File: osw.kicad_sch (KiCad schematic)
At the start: 59 parts, among them J1 Conn_01x02, J2 microSD_MEM2067-02-180-00-A_R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, J3 2169890001, Q1 Q_NMOS_ToshibaSMD, SW1 SPST_EVQ-P7J01P, SW2 SPST_EVQ-P7J01P, SW3 SPST_EVQ-P7J01P, SW4 SPST_EVQ-P7J01P, U1 L96-M33, U10 BMA400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

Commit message: working on the layout.
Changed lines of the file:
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@@
-    (stroke (width 0) (type default))
-  )
-  (wire (pts (xy 88 105) (xy 88 107))
-    (stroke (width 0) (type default))
-  )
-  (wire (pts (xy 88 119) (xy 88 121))
     (stroke (width 0) (type default))
   )

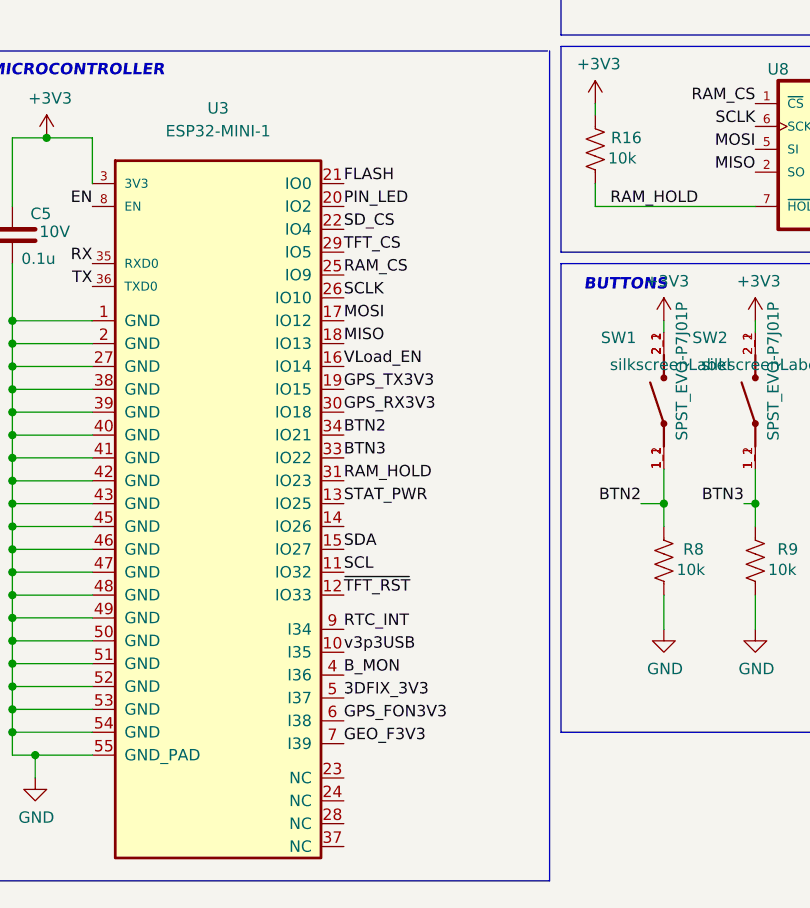
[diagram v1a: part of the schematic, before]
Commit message: Repinned out the ESP32 to get a bit better layout.
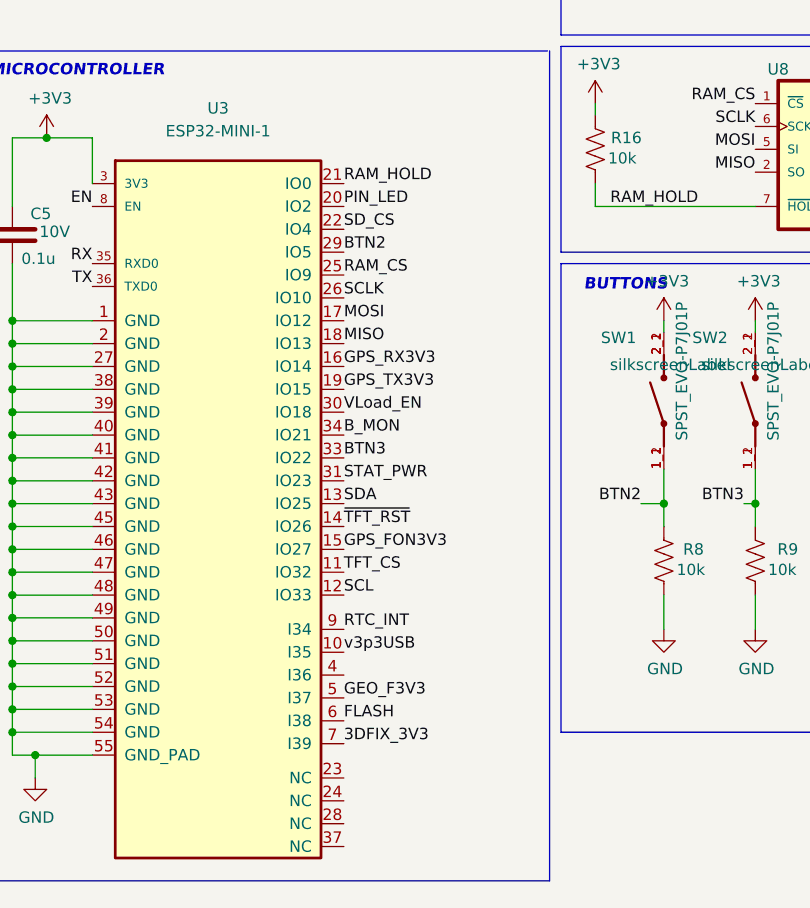
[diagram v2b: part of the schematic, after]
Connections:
- net 3DFIX_3V3: now also U3.7 (I39); no longer U3.5 (I37)
- net BTN2: now also U3.29 (IO5); no longer U3.34 (IO21)
- net B_MON: now also U3.34 (IO21); no longer U3.4 (I36)
- net FLASH: now also U3.6 (I38); no longer U3.21 (IO0)
- net GEO_F3V3: now also U3.5 (I37); no longer U3.7 (I39)
- net GPS_FON3V3: now also U3.15 (IO27); no longer U3.6 (I38)
- net GPS_RX3V3: now also U3.16 (IO14); no longer U3.30 (IO18)
- net RAM_HOLD: now also U3.21 (IO0); no longer U3.31 (IO23)
- net SCL: now also U3.12 (IO33); no longer U3.11 (IO32)
- net SDA: now also U3.13 (IO25); no longer U3.15 (IO27)
- net STAT_PWR: now also U3.31 (IO23); no longer U3.13 (IO25)
- net TFT_CS: now also U3.11 (IO32); no longer U3.29 (IO5)
- net VLoad_EN: now also U3.30 (IO18); no longer U3.16 (IO14)
- net ~{TFT_RST}: now also U3.14 (IO26); no longer U3.12 (IO33)
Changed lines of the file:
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@@
     (effects (font (size 1.27 1.27) (thickness 0.254) bold italic) (justify left bottom))
   )
-  (label "~{TFT_RST}" (at 119.38 124.46 0) (fields_autoplaced)
+  (label "~{TFT_RST}" (at 119.38 116.84 0) (fields_autoplaced)
     (effects (font (size 1.27 1.27)) (justify left bottom))
   )
@@
     (effects (font (size 1.27 1.27)) (justify left bottom))
   )
-  (label "SDA" (at 119.38 119.38 0) (fields_autoplaced)
+  (label "SDA" (at 119.38 114.3 0) (fields_autoplaced)
     (effects (font (size 1.27 1.27)) (justify left bottom))
   )
@@
     (effects (font (size 1.27 1.27)) (justify left bottom))
   )
-  (label "3DFIX_3V3" (at 119.38 135.89 0) (fields_autoplaced)
+  (label "3DFIX_3V3" (at 119.38 140.97 0) (fields_autoplaced)
     (effects (font (size 1.27 1.27)) (justify left bottom))
   )
@@
     (effects (font (size 1.27 1.27)) (justify right bottom))
   )
-  (label "B_MON" (at 119.38 133.35 0) (fields_autoplaced)
+  (label "B_MON" (at 119.38 106.68 0) (fields_autoplaced)
     (effects (font (size 1.27 1.27)) (justify left bottom))
   )
@@
     (effects (font (size 1.27 1.27)) (justify right bottom))
   )
-  (label "VLoad_EN" (at 119.38 99.06 0) (fields_autoplaced)
-    (effects (font (size 1.27 1.27)) (justify left bottom))
-  )
-  (label "GPS_FON3V3" (at 119.38 138.43 0) (fields_autoplaced)
+  (label "VLoad_EN" (at 119.38 104.14 0) (fields_autoplaced)
+    (effects (font (size 1.27 1.27)) (justify left bottom))
+  )
+  (label "GPS_FON3V3" (at 119.38 119.38 0) (fields_autoplaced)
     (effects (font (size 1.27 1.27)) (justify left bottom))
   )
@@
     (effects (font (size 1.27 1.27)) (justify right bottom))
   )
-  (label "SCL" (at 119.38 121.92 0) (fields_autoplaced)
-    (effects (font (size 1.27 1.27)) (justify left bottom))
-  )
-  (label "GEO_F3V3" (at 119.38 140.97 0) (fields_autoplaced)
+  (label "SCL" (at 119.38 124.46 0) (fields_autoplaced)
+    (effects (font (size 1.27 1.27)) (justify left bottom))
+  )
+  (label "GEO_F3V3" (at 119.38 135.89 0) (fields_autoplaced)
     (effects (font (size 1.27 1.27)) (justify left bottom))
   )
@@
     (effects (font (size 1.27 1.27)) (justify left bottom))
   )
-  (label "GPS_RX3V3" (at 119.38 104.14 0) (fields_autoplaced)
+  (label "GPS_RX3V3" (at 119.38 99.06 0) (fields_autoplaced)
     (effects (font (size 1.27 1.27)) (justify left bottom))
   )
@@
     (effects (font (size 1.27 1.27)) (justify right bottom))
   )
-  (label "TFT_CS" (at 119.38 86.36 0) (fields_autoplaced)
+  (label "TFT_CS" (at 119.38 121.92 0) (fields_autoplaced)
     (effects (font (size 1.27 1.27)) (justify left bottom))
   )
@@
     (effects (font (size 1.27 1.27)) (justify right bottom))
   )
-  (label "RAM_HOLD" (at 119.38 111.76 0) (fields_autoplaced)
+  (label "RAM_HOLD" (at 119.38 78.74 0) (fields_autoplaced)
     (effects (font (size 1.27 1.27)) (justify left bottom))
   )
@@
     (effects (font (size 1.27 1.27)) (justify left bottom))
   )
-  (label "STAT_PWR" (at 119.38 114.3 0) (fields_autoplaced)
+  (label "STAT_PWR" (at 119.38 111.76 0) (fields_autoplaced)
     (effects (font (size 1.27 1.27)) (justify left bottom))
   )
@@
     (effects (font (size 1.27 1.27)) (justify right bottom))
   )
-  (label "FLASH" (at 119.38 78.74 0) (fields_autoplaced)
+  (label "FLASH" (at 119.38 138.43 0) (fields_autoplaced)
     (effects (font (size 1.27 1.27)) (justify left bottom))
   )
@@
     (effects (font (size 1.27 1.27)) (justify left bottom))
   )
-  (label "BTN2" (at 119.38 106.68 0) (fields_autoplaced)
-    (effects (font (size 1.27 1.27)) (justify left bottom))
-  )
+  (label "BTN2" (at 119.38 86.36 0) (fields_autoplaced)
+    (effects (font (size 1.27 1.27)) (justify left bottom))
+  )

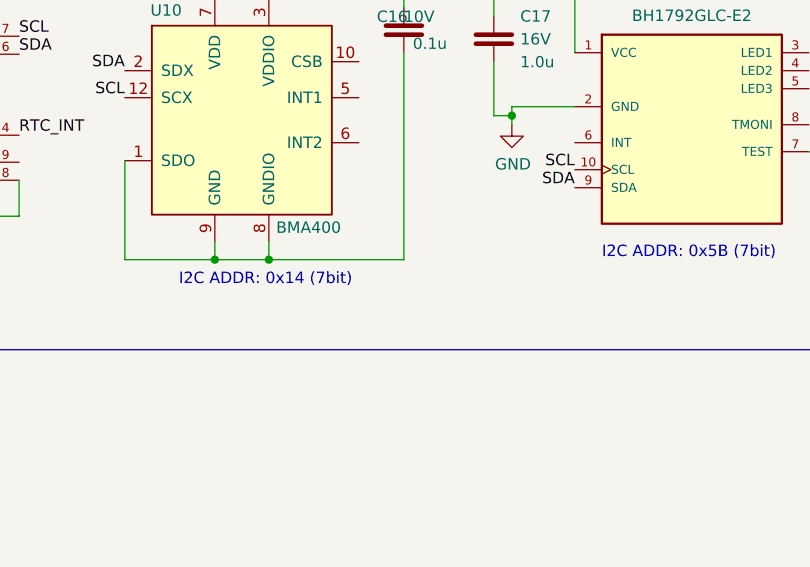
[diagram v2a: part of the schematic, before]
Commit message: Updates to several footprints as they were not quite correct.  Finished layout.  All done on a simple two layer board.  Need to look over the design once more before ordering prototypes.
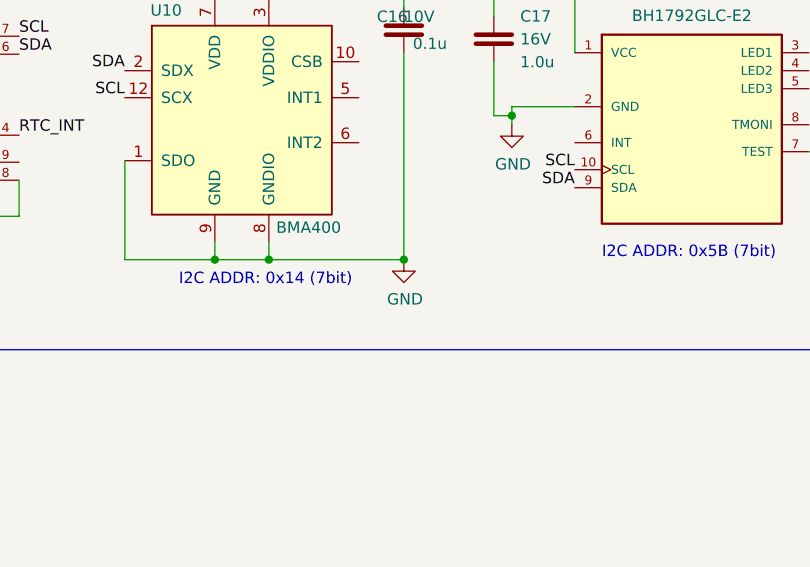
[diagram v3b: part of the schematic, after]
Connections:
- net GND: now also C16.2, U10.1 (SDO), U10.8 (GNDIO), U10.9 (GND)
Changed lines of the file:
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@@
   (junction (at 378.46 210.82) (diameter 0) (color 0 0 0 0)
   )
+  (junction (at 316 223) (diameter 0) (color 0 0 0 0)
+  )
   (junction (at 215.9 86.36) (diameter 0) (color 0 0 0 0)
   )
@@
         )
       )
+    )
+  )
+  (symbol (lib_id "power:GND") (at 316 223 0) (unit 1)
+    (in_bom yes) (on_board yes) (dnp no)
+    (property "Reference" "#PWR01" (at 316 229.35 0)
+      (effects (font (size 1.27 1.27)) hide)
+    )
+    (property "Value" "GND" (at 316.127 227.3942 0)
+      (effects (font (size 1.27 1.27)))
+    )
+    (property "Footprint" "" (at 316 223 0)
+      (effects (font (size 1.27 1.27)) hide)
+    )
+    (property "Datasheet" "" (at 316 223 0)
+      (effects (font (size 1.27 1.27)) hide)
+    )
+    (pin "1")
+    (instances
+      (project "osw"
+        (path "/670ee7c3-0d83-4e97-8079-4c64eeea67de"
+          (reference "#PWR01") (unit 1)
+        )
+      )

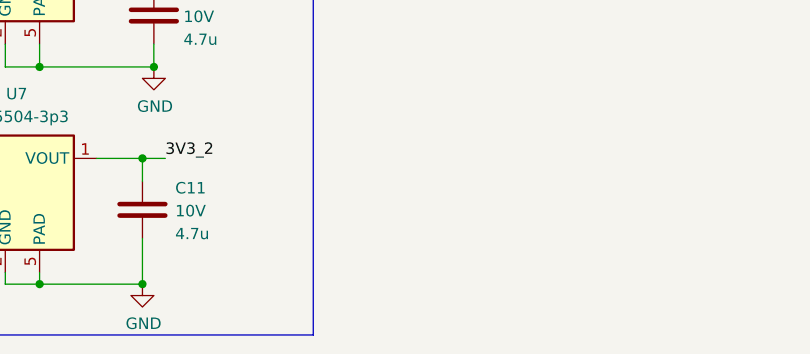
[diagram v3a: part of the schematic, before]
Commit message: Adding some silkscreen dressup.
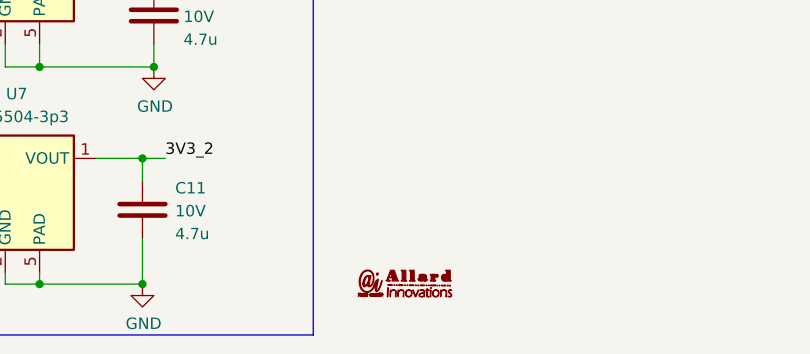
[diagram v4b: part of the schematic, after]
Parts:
- added G1: LOGO, AllardFootPrints:aiLogo, symbol AI_logo:LOGO
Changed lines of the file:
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@@
+    )
+  )
+  (symbol (lib_id "AI_logo:LOGO") (at 189.23 260.35 0) (unit 1)
+    (in_bom no) (on_board yes) (dnp no) (fields_autoplaced)
+    (property "Reference" "G1" (at 189.23 259.2017 0)
+      (effects (font (size 1.27 1.27)) hide)
+    )
+    (property "Value" "LOGO" (at 189.23 261.4983 0)
+      (effects (font (size 1.27 1.27)) hide)
+    )
+    (property "Footprint" "AllardFootPrints:aiLogo" (at 189.23 260.35 0)
+      (effects (font (size 1.27 1.27)) hide)
+    )
+    (property "Datasheet" "" (at 189.23 260.35 0)
+      (effects (font (size 1.27 1.27)) hide)
+    )
+    (instances
+      (project "osw"
+        (path "/670ee7c3-0d83-4e97-8079-4c64eeea67de"
+          (reference "G1") (unit 1)
+        )
+      )
     )
   )

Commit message: Finishing up the board.  Provided nothing jumps out looking through the DOCs later this should be good to order
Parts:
- J1: DigiKey_PN (none) -> 455-B2B-EH-A-ND; MPN (none) -> B2B-EH-A
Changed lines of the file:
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@@
       (effects (font (size 1.27 1.27)) hide)
     )
-    (property "Datasheet" "~" (at 193.675 151.765 0)
+    (property "Datasheet" "https://www.jst-mfg.com/product/pdf/eng/eEH.pdf" (at 193.675 151.765 0)
       (effects (font (size 1.27 1.27)) hide)
     )
+    (property "DigiKey_PN" "455-B2B-EH-A-ND" (at 193.675 151.765 0)
+      (effects (font (size 1.27 1.27)) hide)
+    )
+    (property "MPN" "B2B-EH-A" (at 193.675 151.765 0)
+      (effects (font (size 1.27 1.27)) hide)
+    )

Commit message: Updates for final fab
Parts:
- J1: Manufacturer (none) -> JST
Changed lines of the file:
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@@
+      (effects (font (size 1.27 1.27)) hide)
+    )
+    (property "Manufacturer" "JST" (at 193.675 151.765 0)
       (effects (font (size 1.27 1.27)) hide)
     )

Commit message: Corrected a library FP.  Also corrected the fact the regulators need to be pulled up to work correctly.  Rotated LCD FP so it folds correctly now.  Only thing left is to find the nasty short that is causing me issues.
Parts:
- U11: footprint open-Smartwatch:GC9A01_IPS_display -> open-Smartwatch:GC9A01_IPS_display_under
- U8: symbol open-Smartwatch:23K256-I/SN -> open-Smartwatch:23K256-I/SN
- U9: symbol open-Smartwatch:PCF85063ATL/1,118 -> open-Smartwatch:PCF85063ATL/1,118
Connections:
- net PIN_LED: now also U3.14 (IO26); no longer U3.20 (IO2)
- net VCC: now also U5.3 (EN)
- net VCC_SW: now also U7.3 (EN)
- net ~{TFT_RST}: now also U3.20 (IO2); no longer U3.14 (IO26)
- no-connect marks 4 -> 3
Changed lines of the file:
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@@
   )
   (no_connect (at 294 33))
-  (no_connect (at 137.05 224.79))
   (no_connect (at 71 232))
   (no_connect (at 294 36))
@@
     (stroke (width 0) (type default))
   )
+  (wire (pts (xy 137.16 220.98) (xy 137.16 224.79))
+    (stroke (width 0) (type default))
+  )
   (polyline (pts (xy 247 115) (xy 296 115))
     (stroke (width 0) (type default))
@@
     (stroke (width 0) (type default))
   )
+  (wire (pts (xy 137.16 246.38) (xy 137.16 250.19))
+    (stroke (width 0) (type default))
+  )
   (wire (pts (xy 291 28) (xy 291 26))
     (stroke (width 0) (type default))
@@
     (effects (font (size 1.27 1.27) (thickness 0.254) bold italic) (justify left bottom))
   )
-  (label "~{TFT_RST}" (at 119.38 116.84 0) (fields_autoplaced)
+  (label "~{TFT_RST}" (at 119.38 81.28 0) (fields_autoplaced)
     (effects (font (size 1.27 1.27)) (justify left bottom))
   )
@@
     (effects (font (size 1.27 1.27)) (justify right bottom))
   )
-  (label "PIN_LED" (at 119.38 81.28 0) (fields_autoplaced)
+  (label "PIN_LED" (at 119.38 116.84 0) (fields_autoplaced)
     (effects (font (size 1.27 1.27)) (justify left bottom))
   )
@@
       (effects (font (size 1.27 1.27)) (justify left))
     )
-    (property "Footprint" "open-Smartwatch:GC9A01_IPS_display" (at 191.77 62.23 0)
+    (property "Footprint" "open-Smartwatch:GC9A01_IPS_display_under" (at 191.77 62.23 0)
       (effects (font (size 1.27 1.27)) hide)
     )
@@
     )
   )
-  (symbol (lib_id "open-Smartwatch:PCF85063ATL{slash}1,118") (at 260.245 206.17 0) (unit 1)
+  (symbol (lib_id "open-Smartwatch:PCF85063ATL/1,118") (at 260.245 206.17 0) (unit 1)
     (in_bom yes) (on_board yes) (dnp no) (fields_autoplaced)
     (property "Reference" "U9" (at 260.245 191.49 0)
@@
     )
   )
-  (symbol (lib_id "open-Smartwatch:23K256-I{slash}SN") (at 175.26 76.2 0) (mirror y) (unit 1)
+  (symbol (lib_id "open-Smartwatch:23K256-I/SN") (at 175.26 76.2 0) (mirror y) (unit 1)
     (in_bom yes) (on_board yes) (dnp no)
     (property "Reference" "U8" (at 167.64 66.04 0)

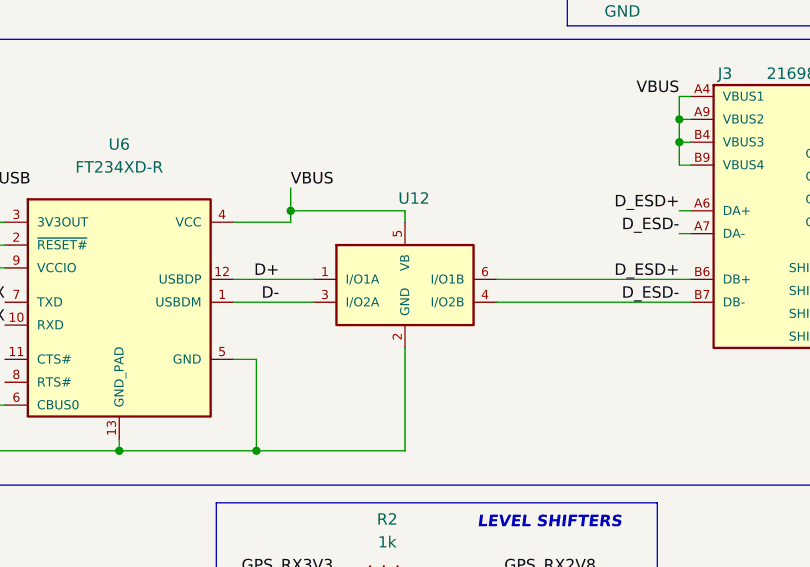
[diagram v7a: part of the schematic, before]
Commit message: Fixing the ESD diode array that was mis-pinned.
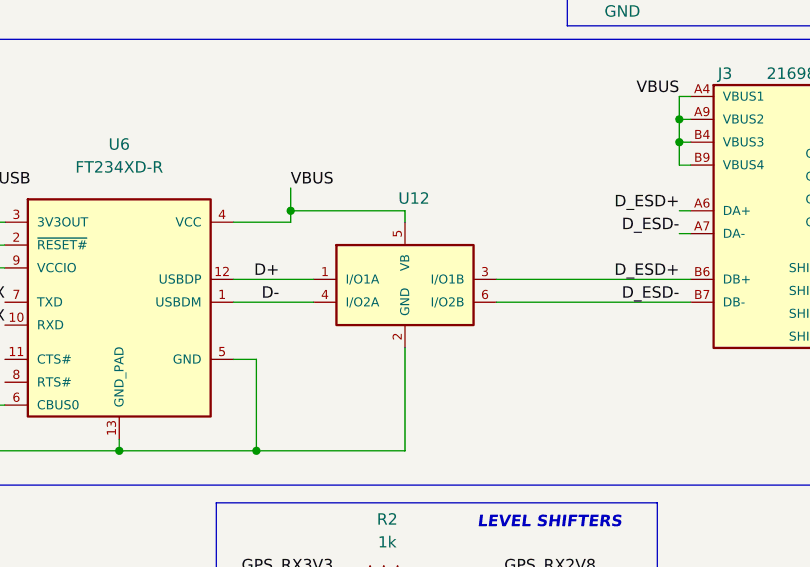
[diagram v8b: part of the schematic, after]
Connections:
- net D-: now also U12.4 (I/O2A); no longer U12.3 (I/O2A)
- net D_ESD+: now also U12.3 (I/O1B); no longer U12.6 (I/O1B)
- net D_ESD-: now also U12.6 (I/O2B); no longer U12.4 (I/O2B)
